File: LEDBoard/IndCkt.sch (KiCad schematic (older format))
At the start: 15 parts

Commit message: more work on the LED board
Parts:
- removed D?: LED-Green, symbol LED
- removed R?: R, symbol R
- D?: value LED-Red -> LED
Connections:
- wire segments 31 -> 27
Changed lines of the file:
@@
 $Descr A4 11693 8268
 encoding utf-8
-Sheet 2 2
+Sheet 7 21
 Title ""
 Date ""
@@
 U 1 1 583A6A3F
 P 3250 1750
+AR Path="/583A699B/583A6A3F" Ref="R?"  Part="1"
+AR Path="/583A8EB9/583A6A3F" Ref="R?"  Part="1"
+AR Path="/583AA7C1/583A6A3F" Ref="R?"  Part="1"
+AR Path="/583ACE7E/583A6A3F" Ref="R?"  Part="1"
 F 0 "R?" V 3330 1750 50  0000 C CNN
 F 1 "R" V 3250 1750 50  0000 C CNN
@@
 U 1 1 583A6A8C
 P 3250 2100
+AR Path="/583A699B/583A6A8C" Ref="R?"  Part="1"
+AR Path="/583A8EB9/583A6A8C" Ref="R?"  Part="1"
+AR Path="/583AA7C1/583A6A8C" Ref="R?"  Part="1"
+AR Path="/583ACE7E/583A6A8C" Ref="R?"  Part="1"
 F 0 "R?" V 3330 2100 50  0000 C CNN
 F 1 "R" V 3250 2100 50  0000 C CNN
@@
 U 1 1 583A6ABA
 P 3250 2450
+AR Path="/583A699B/583A6ABA" Ref="R?"  Part="1"
+AR Path="/583A8EB9/583A6ABA" Ref="R?"  Part="1"
+AR Path="/583AA7C1/583A6ABA" Ref="R?"  Part="1"
+AR Path="/583ACE7E/583A6ABA" Ref="R?"  Part="1"
 F 0 "R?" V 3330 2450 50  0000 C CNN
 F 1 "R" V 3250 2450 50  0000 C CNN
@@
 U 1 1 583A6ADB
 P 4200 3200
+AR Path="/583A699B/583A6ADB" Ref="U?"  Part="1"
+AR Path="/583A8EB9/583A6ADB" Ref="U?"  Part="1"
+AR Path="/583AA7C1/583A6ADB" Ref="U?"  Part="1"
+AR Path="/583ACE7E/583A6ADB" Ref="U?"  Part="1"
 F 0 "U?" H 4350 3350 50  0000 C CNN
 F 1 "LM193" H 4450 3050 50  0000 C CNN
@@
 U 1 1 583A6B4D
 P 3250 3950
+AR Path="/583A699B/583A6B4D" Ref="R?"  Part="1"
+AR Path="/583A8EB9/583A6B4D" Ref="R?"  Part="1"
+AR Path="/583AA7C1/583A6B4D" Ref="R?"  Part="1"
+AR Path="/583ACE7E/583A6B4D" Ref="R?"  Part="1"
 F 0 "R?" V 3330 3950 50  0000 C CNN
 F 1 "R" V 3250 3950 50  0000 C CNN
@@
 U 1 1 583A6B92
 P 3250 4350
+AR Path="/583A699B/583A6B92" Ref="R?"  Part="1"
+AR Path="/583A8EB9/583A6B92" Ref="R?"  Part="1"
+AR Path="/583AA7C1/583A6B92" Ref="R?"  Part="1"
+AR Path="/583ACE7E/583A6B92" Ref="R?"  Part="1"
 F 0 "R?" V 3330 4350 50  0000 C CNN
 F 1 "R" V 3250 4350 50  0000 C CNN
@@
 U 1 1 583A6BB8
 P 3250 4700
+AR Path="/583A699B/583A6BB8" Ref="R?"  Part="1"
+AR Path="/583A8EB9/583A6BB8" Ref="R?"  Part="1"
+AR Path="/583AA7C1/583A6BB8" Ref="R?"  Part="1"
+AR Path="/583ACE7E/583A6BB8" Ref="R?"  Part="1"
 F 0 "R?" V 3330 4700 50  0000 C CNN
 F 1 "R" V 3250 4700 50  0000 C CNN
@@
 U 1 1 583A6BE7
 P 4500 3950
+AR Path="/583A699B/583A6BE7" Ref="R?"  Part="1"
+AR Path="/583A8EB9/583A6BE7" Ref="R?"  Part="1"
+AR Path="/583AA7C1/583A6BE7" Ref="R?"  Part="1"
+AR Path="/583ACE7E/583A6BE7" Ref="R?"  Part="1"
 F 0 "R?" V 4580 3950 50  0000 C CNN
 F 1 "R" V 4500 3950 50  0000 C CNN
@@
 U 1 1 583A6C2D
 P 4500 2450
+AR Path="/583A699B/583A6C2D" Ref="R?"  Part="1"
+AR Path="/583A8EB9/583A6C2D" Ref="R?"  Part="1"
+AR Path="/583AA7C1/583A6C2D" Ref="R?"  Part="1"
+AR Path="/583ACE7E/583A6C2D" Ref="R?"  Part="1"
 F 0 "R?" V 4580 2450 50  0000 C CNN
 F 1 "R" V 4500 2450 50  0000 C CNN
@@
 U 1 1 583A6CF9
 P 2950 2550
+AR Path="/583A699B/583A6CF9" Ref="#PWR?"  Part="1"
+AR Path="/583A8EB9/583A6CF9" Ref="#PWR?"  Part="1"
+AR Path="/583AA7C1/583A6CF9" Ref="#PWR?"  Part="1"
+AR Path="/583ACE7E/583A6CF9" Ref="#PWR?"  Part="1"
 F 0 "#PWR?" H 2950 2300 50  0001 C CNN
 F 1 "GND" H 2950 2400 50  0000 C CNN
@@
 U 1 1 583A6D38
 P 2850 4850
+AR Path="/583A699B/583A6D38" Ref="#PWR?"  Part="1"
+AR Path="/583A8EB9/583A6D38" Ref="#PWR?"  Part="1"
+AR Path="/583AA7C1/583A6D38" Ref="#PWR?"  Part="1"
+AR Path="/583ACE7E/583A6D38" Ref="#PWR?"  Part="1"
 F 0 "#PWR?" H 2850 4600 50  0001 C CNN
 F 1 "GND" H 2850 4700 50  0000 C CNN
@@
 U 1 1 583A6EC0
 P 4100 2750
+AR Path="/583A699B/583A6EC0" Ref="#PWR?"  Part="1"
+AR Path="/583A8EB9/583A6EC0" Ref="#PWR?"  Part="1"
+AR Path="/583AA7C1/583A6EC0" Ref="#PWR?"  Part="1"
+AR Path="/583ACE7E/583A6EC0" Ref="#PWR?"  Part="1"
 F 0 "#PWR?" H 4100 2600 50  0001 C CNN
 F 1 "VCC" H 4100 2900 50  0000 C CNN
@@
 U 1 1 583A6EE6
 P 4100 3650
+AR Path="/583A699B/583A6EE6" Ref="#PWR?"  Part="1"
+AR Path="/583A8EB9/583A6EE6" Ref="#PWR?"  Part="1"
+AR Path="/583AA7C1/583A6EE6" Ref="#PWR?"  Part="1"
+AR Path="/583ACE7E/583A6EE6" Ref="#PWR?"  Part="1"
 F 0 "#PWR?" H 4100 3400 50  0001 C CNN
 F 1 "GND" H 4100 3500 50  0000 C CNN
@@
 U 1 1 583A77A3
 P 1400 1550
+AR Path="/583A699B/583A77A3" Ref="R?"  Part="1"
+AR Path="/583A8EB9/583A77A3" Ref="R?"  Part="1"
+AR Path="/583AA7C1/583A77A3" Ref="R?"  Part="1"
+AR Path="/583ACE7E/583A77A3" Ref="R?"  Part="1"
 F 0 "R?" V 1480 1550 50  0000 C CNN
 F 1 "R" V 1400 1550 50  0000 C CNN
@@
 U 1 1 583A77F6
 P 1400 2500
+AR Path="/583A699B/583A77F6" Ref="R?"  Part="1"
+AR Path="/583A8EB9/583A77F6" Ref="R?"  Part="1"
+AR Path="/583AA7C1/583A77F6" Ref="R?"  Part="1"
+AR Path="/583ACE7E/583A77F6" Ref="R?"  Part="1"
 F 0 "R?" V 1480 2500 50  0000 C CNN
 F 1 "R" V 1400 2500 50  0000 C CNN
@@
 U 1 1 583A790B
 P 1400 1100
+AR Path="/583A699B/583A790B" Ref="#PWR?"  Part="1"
+AR Path="/583A8EB9/583A790B" Ref="#PWR?"  Part="1"
+AR Path="/583AA7C1/583A790B" Ref="#PWR?"  Part="1"
+AR Path="/583ACE7E/583A790B" Ref="#PWR?"  Part="1"
 F 0 "#PWR?" H 1400 950 50  0001 C CNN
 F 1 "VCC" H 1400 1250 50  0000 C CNN
@@
 U 1 1 583A7935
 P 1400 3100
+AR Path="/583A699B/583A7935" Ref="#PWR?"  Part="1"
+AR Path="/583A8EB9/583A7935" Ref="#PWR?"  Part="1"
+AR Path="/583AA7C1/583A7935" Ref="#PWR?"  Part="1"
+AR Path="/583ACE7E/583A7935" Ref="#PWR?"  Part="1"
 F 0 "#PWR?" H 1400 2850 50  0001 C CNN
 F 1 "GND" H 1400 2950 50  0000 C CNN
@@
 U 1 1 583A81F1
 P 7300 3200
+AR Path="/583A8EB9/583A81F1" Ref="D?"  Part="1"
+AR Path="/583A699B/583A81F1" Ref="D?"  Part="1"
+AR Path="/583AA7C1/583A81F1" Ref="D?"  Part="1"
+AR Path="/583ACE7E/583A81F1" Ref="D?"  Part="1"
 F 0 "D?" H 7300 3300 50  0000 C CNN
-F 1 "LED-Red" H 7300 3100 50  0000 C CNN
+F 1 "LED" H 7300 3100 50  0000 C CNN
 F 2 "" H 7300 3200 50  0000 C CNN
 F 3 "" H 7300 3200 50  0000 C CNN
@@
 U 1 1 583A81F8
 P 8050 3200
+AR Path="/583A8EB9/583A81F8" Ref="R?"  Part="1"
+AR Path="/583A699B/583A81F8" Ref="R?"  Part="1"
+AR Path="/583AA7C1/583A81F8" Ref="R?"  Part="1"
+AR Path="/583ACE7E/583A81F8" Ref="R?"  Part="1"
 F 0 "R?" V 8130 3200 50  0000 C CNN
 F 1 "R" V 8050 3200 50  0000 C CNN
@@
 U 1 1 583A8202
 P 8600 3200
+AR Path="/583A8EB9/583A8202" Ref="#PWR?"  Part="1"
+AR Path="/583A699B/583A8202" Ref="#PWR?"  Part="1"
+AR Path="/583AA7C1/583A8202" Ref="#PWR?"  Part="1"
+AR Path="/583ACE7E/583A8202" Ref="#PWR?"  Part="1"
 F 0 "#PWR?" H 8600 3050 50  0001 C CNN
 F 1 "VCC" H 8600 3350 50  0000 C CNN
@@
 	0    1    1    0
 $EndComp
-$Comp
-L R R?
-U 1 1 583A8208
-P 8050 2900
-F 0 "R?" V 8130 2900 50  0000 C CNN
-F 1 "R" V 8050 2900 50  0000 C CNN
-F 2 "" V 7980 2900 50  0000 C CNN
-F 3 "" H 8050 2900 50  0000 C CNN
-	1    8050 2900
-	0    1    1    0
-$EndComp
-$Comp
-L LED D?
-U 1 1 583A820F
-P 7550 2900
-F 0 "D?" H 7550 3000 50  0000 C CNN
-F 1 "LED-Green" H 7550 2800 50  0000 C CNN
-F 2 "" H 7550 2900 50  0000 C CNN
-F 3 "" H 7550 2900 50  0000 C CNN
-	1    7550 2900
-	1    0    0    -1
-$EndComp
-$Comp
-L GND #PWR?
-U 1 1 583A8216
-P 7250 2900
-F 0 "#PWR?" H 7250 2650 50  0001 C CNN
-F 1 "GND" H 7250 2750 50  0000 C CNN
-F 2 "" H 7250 2900 50  0000 C CNN
-F 3 "" H 7250 2900 50  0000 C CNN
-	1    7250 2900
-	0    1    1    0
-$EndComp
-Wire Wire Line
-	8400 3200 8400 2900
-Wire Wire Line
-	8400 2900 8200 2900
 Connection ~ 8400 3200
-Wire Wire Line
-	7900 2900 7750 2900
-Wire Wire Line
-	7350 2900 7250 2900
 Text HLabel 6650 3200 0    60   Input ~ 0
 Vout

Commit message: Added the power switching device and wiring between the pod batteries and backup batteries
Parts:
- removed R? (x10): R, symbol R
- removed U?: LM193, symbol LM193
- added R15, R16, R17, R18, R19, R20, R21, R22, R23, R24, R25, R26: R, Resistors_SMD:R_1206_HandSoldering, symbol R
- added U2: LEDboardcomparator, TO_SOT_Packages_SMD:SOT-23-5, symbol LEDboardcomparator
- D2: renamed from D?; footprint (none) -> LEDs:LED_1206
- R14: renamed from R?; footprint (none) -> Resistors_SMD:R_1206_HandSoldering
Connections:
- net labels added: Vin_div
- wire segments 27 -> 35

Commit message: made major changed to the led board mostly dealing with schematic
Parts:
- renumbered D2 to D201, R14 to R201, R15 to R202, R16 to R203, R17 to R204, R18 to R205, R19 to R206, R20 to R207, R21 to R208, R22 to R209, R23 to R210, R24 to R211, R25 to R212, R26 to R213, U2 to U201

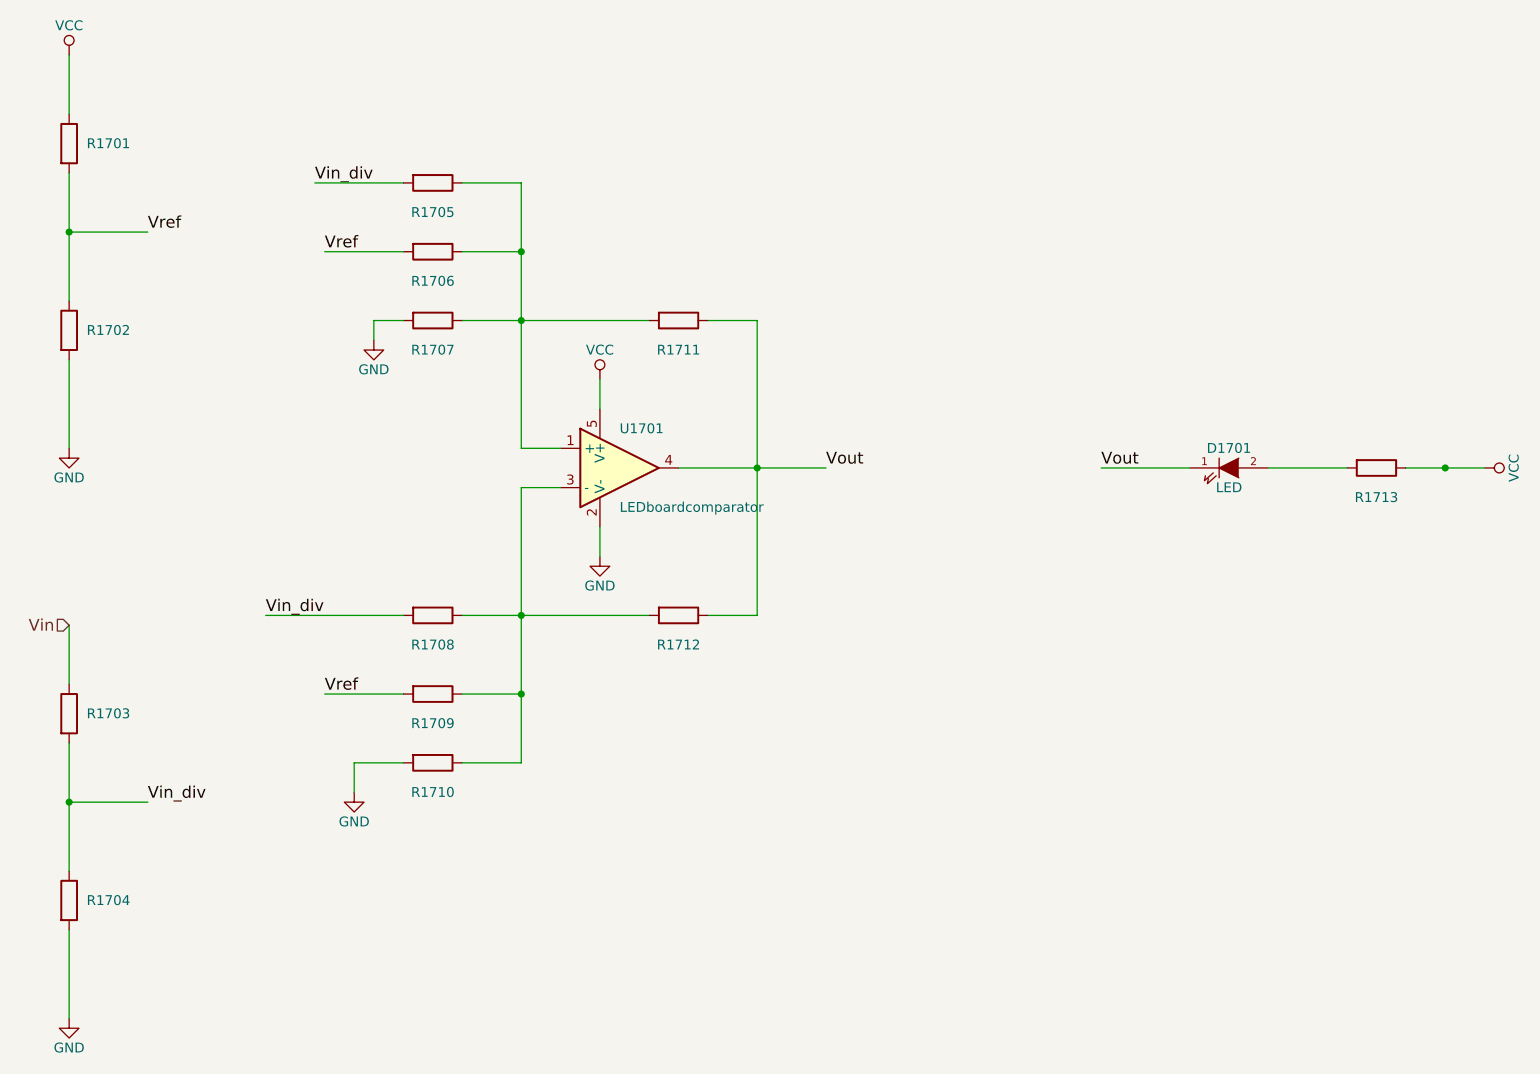
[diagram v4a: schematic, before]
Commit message: added more modules to the Led board and put in the circuit for the cool switch and the Led that goes along with it. Also made some more changes to the sensors and which ones we are going to have
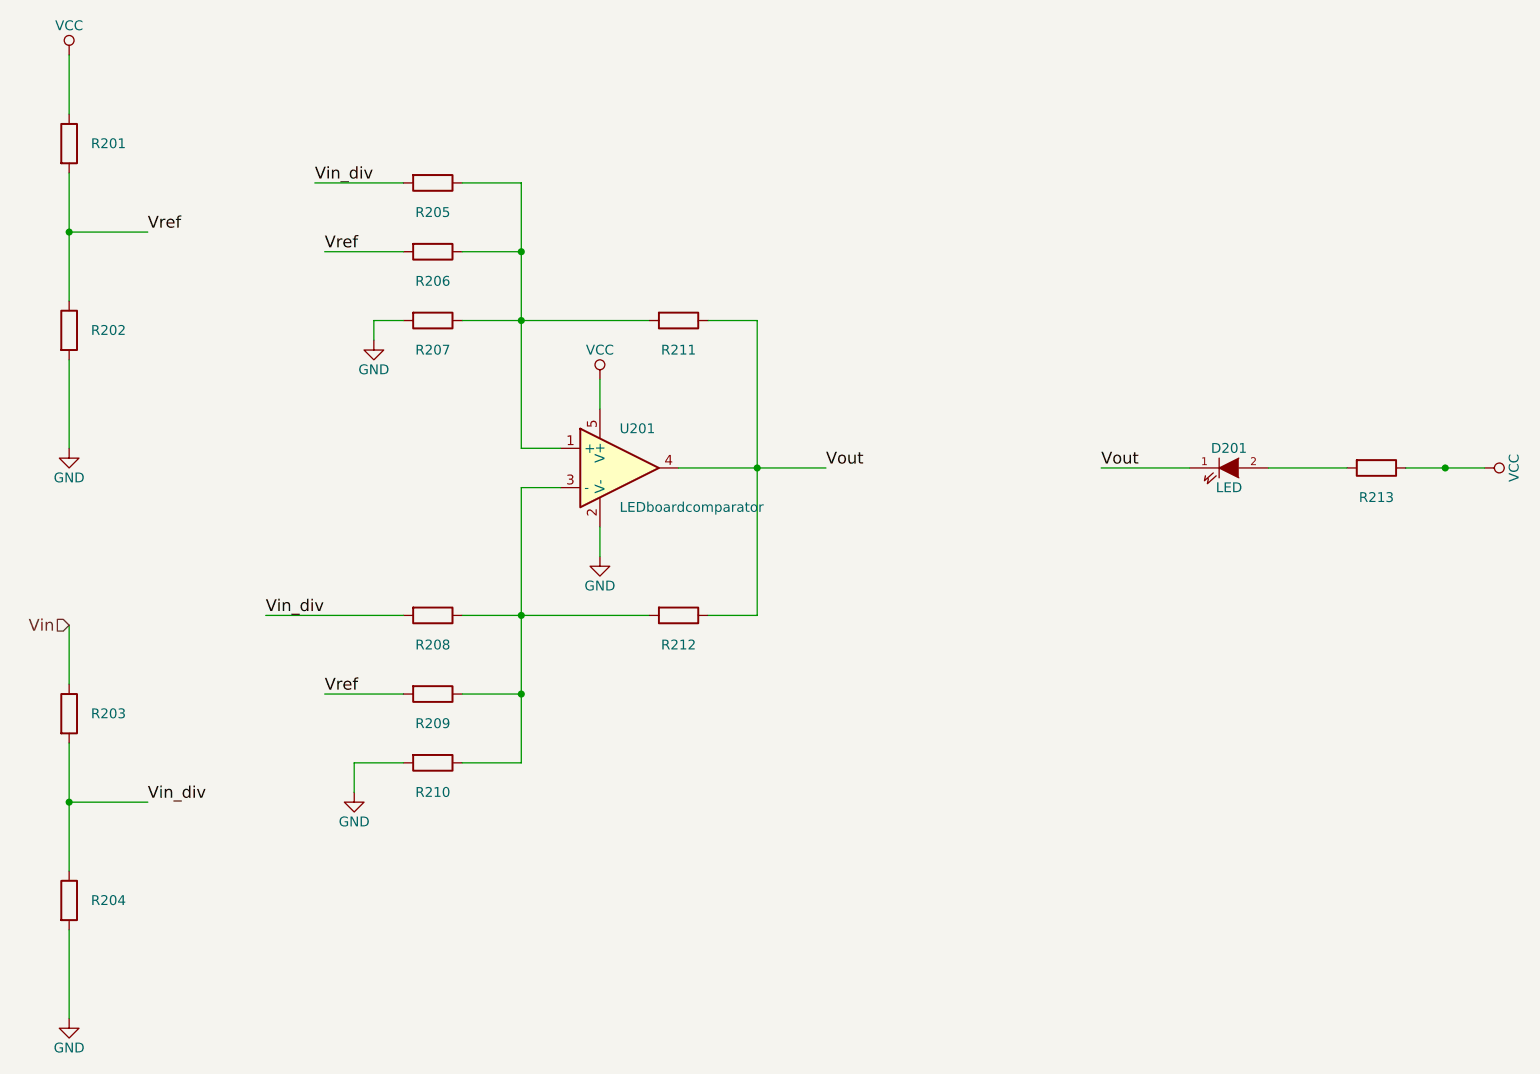
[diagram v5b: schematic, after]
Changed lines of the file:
@@
 $Descr A4 11693 8268
 encoding utf-8
-Sheet 14 18
+Sheet 2 22
 Title ""
 Date ""
@@
 AR Path="/583AD5CE/583A6CF9" Ref="#PWR0126"  Part="1"
 AR Path="/583AD5D1/583A6CF9" Ref="#PWR0134"  Part="1"
-F 0 "#PWR0134" H 2950 2300 50  0001 C CNN
+F 0 "#PWR014" H 2950 2300 50  0001 C CNN
 F 1 "GND" H 2950 2400 50  0000 C CNN
 F 2 "" H 2950 2550 50  0000 C CNN
@@
 AR Path="/583AD5CE/583A6D38" Ref="#PWR0127"  Part="1"
 AR Path="/583AD5D1/583A6D38" Ref="#PWR0135"  Part="1"
-F 0 "#PWR0135" H 2850 4600 50  0001 C CNN
+F 0 "#PWR015" H 2850 4600 50  0001 C CNN
 F 1 "GND" H 2850 4700 50  0000 C CNN
 F 2 "" H 2850 4850 50  0000 C CNN
@@
 AR Path="/583AD5CE/583A6EC0" Ref="#PWR0128"  Part="1"
 AR Path="/583AD5D1/583A6EC0" Ref="#PWR0136"  Part="1"
-F 0 "#PWR0136" H 4100 2600 50  0001 C CNN
+F 0 "#PWR016" H 4100 2600 50  0001 C CNN
 F 1 "VCC" H 4100 2900 50  0000 C CNN
 F 2 "" H 4100 2750 50  0000 C CNN
@@
 AR Path="/583AD5CE/583A6EE6" Ref="#PWR0129"  Part="1"
 AR Path="/583AD5D1/583A6EE6" Ref="#PWR0137"  Part="1"
-F 0 "#PWR0137" H 4100 3400 50  0001 C CNN
+F 0 "#PWR017" H 4100 3400 50  0001 C CNN
 F 1 "GND" H 4100 3500 50  0000 C CNN
 F 2 "" H 4100 3650 50  0000 C CNN
@@
 AR Path="/583AD5CE/583A77A3" Ref="R1601"  Part="1"
 AR Path="/583AD5D1/583A77A3" Ref="R1701"  Part="1"
-F 0 "R1701" H 1600 1550 50  0000 C CNN
+F 0 "R201" H 1600 1550 50  0000 C CNN
 F 1 "R" V 1400 1550 50  0001 C CNN
 F 2 "Resistors_SMD:R_1206_HandSoldering" V 1330 1550 50  0001 C CNN
@@
 AR Path="/583AD5CE/583A790B" Ref="#PWR0130"  Part="1"
 AR Path="/583AD5D1/583A790B" Ref="#PWR0138"  Part="1"
-F 0 "#PWR0138" H 1400 950 50  0001 C CNN
+F 0 "#PWR018" H 1400 950 50  0001 C CNN
 F 1 "VCC" H 1400 1250 50  0000 C CNN
 F 2 "" H 1400 1100 50  0000 C CNN
@@
 AR Path="/583AD5CE/583A7935" Ref="#PWR0131"  Part="1"
 AR Path="/583AD5D1/583A7935" Ref="#PWR0139"  Part="1"
-F 0 "#PWR0139" H 1400 2850 50  0001 C CNN
+F 0 "#PWR019" H 1400 2850 50  0001 C CNN
 F 1 "GND" H 1400 2950 50  0000 C CNN
 F 2 "" H 1400 3100 50  0000 C CNN
@@
 AR Path="/583AD5CE/583A81F1" Ref="D1601"  Part="1"
 AR Path="/583AD5D1/583A81F1" Ref="D1701"  Part="1"
-F 0 "D1701" H 7300 3300 50  0000 C CNN
+F 0 "D201" H 7300 3300 50  0000 C CNN
 F 1 "LED" H 7300 3100 50  0000 C CNN
 F 2 "LEDs:LED_1206" H 7300 3200 50  0001 C CNN
@@
 AR Path="/583AD5CE/583A8202" Ref="#PWR0132"  Part="1"
 AR Path="/583AD5D1/583A8202" Ref="#PWR0140"  Part="1"
-F 0 "#PWR0140" H 8600 3050 50  0001 C CNN
+F 0 "#PWR020" H 8600 3050 50  0001 C CNN
 F 1 "VCC" H 8600 3350 50  0000 C CNN
 F 2 "" H 8600 3200 50  0000 C CNN
@@
 AR Path="/583AD5CE/583CFC0B" Ref="#PWR0133"  Part="1"
 AR Path="/583AD5D1/583CFC0B" Ref="#PWR0141"  Part="1"
-F 0 "#PWR0141" H 1400 5750 50  0001 C CNN
+F 0 "#PWR021" H 1400 5750 50  0001 C CNN
 F 1 "GND" H 1400 5850 50  0000 C CNN
 F 2 "" H 1400 6000 50  0000 C CNN
@@
 AR Path="/583AD5CE/583D0F65" Ref="R1602"  Part="1"
 AR Path="/583AD5D1/583D0F65" Ref="R1702"  Part="1"
-F 0 "R1702" H 1600 2500 50  0000 C CNN
+F 0 "R202" H 1600 2500 50  0000 C CNN
 F 1 "R" V 1400 2500 50  0001 C CNN
 F 2 "Resistors_SMD:R_1206_HandSoldering" V 1330 2500 50  0001 C CNN
@@
 AR Path="/583AD5CE/583D1063" Ref="R1603"  Part="1"
 AR Path="/583AD5D1/583D1063" Ref="R1703"  Part="1"
-F 0 "R1703" H 1600 4450 50  0000 C CNN
+F 0 "R203" H 1600 4450 50  0000 C CNN
 F 1 "R" V 1400 4450 50  0001 C CNN
 F 2 "Resistors_SMD:R_1206_HandSoldering" V 1330 4450 50  0001 C CNN
@@
 AR Path="/583AD5CE/583D109D" Ref="R1604"  Part="1"
 AR Path="/583AD5D1/583D109D" Ref="R1704"  Part="1"
-F 0 "R1704" H 1600 5400 50  0000 C CNN
+F 0 "R204" H 1600 5400 50  0000 C CNN
 F 1 "R" V 1400 5400 50  0001 C CNN
 F 2 "Resistors_SMD:R_1206_HandSoldering" V 1330 5400 50  0001 C CNN
@@
 AR Path="/583AD5CE/583D10D6" Ref="R1610"  Part="1"
 AR Path="/583AD5D1/583D10D6" Ref="R1710"  Part="1"
-F 0 "R1710" V 3400 4700 50  0000 C CNN
+F 0 "R210" V 3400 4700 50  0000 C CNN
 F 1 "R" V 3250 4700 50  0001 C CNN
 F 2 "Resistors_SMD:R_1206_HandSoldering" V 3180 4700 50  0001 C CNN
@@
 AR Path="/583AD5CE/583D1175" Ref="R1609"  Part="1"
 AR Path="/583AD5D1/583D1175" Ref="R1709"  Part="1"
-F 0 "R1709" V 3400 4350 50  0000 C CNN
+F 0 "R209" V 3400 4350 50  0000 C CNN
 F 1 "R" V 3250 4350 50  0001 C CNN
 F 2 "Resistors_SMD:R_1206_HandSoldering" V 3180 4350 50  0001 C CNN
@@
 AR Path="/583AD5CE/583D11AE" Ref="R1608"  Part="1"
 AR Path="/583AD5D1/583D11AE" Ref="R1708"  Part="1"
-F 0 "R1708" V 3400 3950 50  0000 C CNN
+F 0 "R208" V 3400 3950 50  0000 C CNN
 F 1 "R" V 3250 3950 50  0001 C CNN
 F 2 "Resistors_SMD:R_1206_HandSoldering" V 3180 3950 50  0001 C CNN
@@
 AR Path="/583AD5CE/583D1238" Ref="R1611"  Part="1"
 AR Path="/583AD5D1/583D1238" Ref="R1711"  Part="1"
-F 0 "R1711" V 4650 2450 50  0000 C CNN
+F 0 "R211" V 4650 2450 50  0000 C CNN
 F 1 "R" V 4500 2450 50  0001 C CNN
 F 2 "Resistors_SMD:R_1206_HandSoldering" V 4430 2450 50  0001 C CNN
@@
 AR Path="/583AD5CE/583D128B" Ref="R1607"  Part="1"
 AR Path="/583AD5D1/583D128B" Ref="R1707"  Part="1"
-F 0 "R1707" V 3400 2450 50  0000 C CNN
+F 0 "R207" V 3400 2450 50  0000 C CNN
 F 1 "R" V 3250 2450 50  0001 C CNN
 F 2 "Resistors_SMD:R_1206_HandSoldering" V 3180 2450 50  0001 C CNN
@@
 AR Path="/583AD5CE/583D12FD" Ref="R1606"  Part="1"
 AR Path="/583AD5D1/583D12FD" Ref="R1706"  Part="1"
-F 0 "R1706" V 3400 2100 50  0000 C CNN
+F 0 "R206" V 3400 2100 50  0000 C CNN
 F 1 "R" V 3250 2100 50  0001 C CNN
 F 2 "Resistors_SMD:R_1206_HandSoldering" V 3180 2100 50  0001 C CNN
@@
 AR Path="/583AD5CE/583D133E" Ref="R1605"  Part="1"
 AR Path="/583AD5D1/583D133E" Ref="R1705"  Part="1"
-F 0 "R1705" V 3400 1750 50  0000 C CNN
+F 0 "R205" V 3400 1750 50  0000 C CNN
 F 1 "R" V 3250 1750 50  0001 C CNN
 F 2 "Resistors_SMD:R_1206_HandSoldering" V 3180 1750 50  0001 C CNN
@@
 AR Path="/583AD5CE/583D11EC" Ref="R1612"  Part="1"
 AR Path="/583AD5D1/583D11EC" Ref="R1712"  Part="1"
-F 0 "R1712" V 4650 3950 50  0000 C CNN
+F 0 "R212" V 4650 3950 50  0000 C CNN
 F 1 "R" V 4500 3950 50  0001 C CNN
 F 2 "Resistors_SMD:R_1206_HandSoldering" V 4430 3950 50  0001 C CNN
@@
 AR Path="/583AD5CE/5844D27C" Ref="R1613"  Part="1"
 AR Path="/583AD5D1/5844D27C" Ref="R1713"  Part="1"
-F 0 "R1713" V 8200 3200 50  0000 C CNN
+F 0 "R213" V 8200 3200 50  0000 C CNN
 F 1 "R" V 8050 3200 50  0001 C CNN
 F 2 "Resistors_SMD:R_1206_HandSoldering" V 7980 3200 50  0001 C CNN
@@
 AR Path="/583AD5CE/5844E293" Ref="U1601"  Part="1"
 AR Path="/583AD5D1/5844E293" Ref="U1701"  Part="1"
-F 0 "U1701" H 4200 3400 50  0000 L CNN
+F 0 "U201" H 4200 3400 50  0000 L CNN
 F 1 "LEDboardcomparator" H 4200 3000 50  0000 L CNN
 F 2 "TO_SOT_Packages_SMD:SOT-23-5" H 4250 3400 50  0001 C CNN
